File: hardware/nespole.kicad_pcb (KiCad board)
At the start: 2 copper layers, 26.4 x 50.5 mm, 20 parts, among them IC1 ATTINY25-20SSU, J1 Screw_Terminal_1x02, J2 Screw_Terminal_1x02, J3 ICSP, P1 USB_OTG, Q1 IRF510, U1 MAX31855KASA, U2 AP1117, U3 CH340G, Y1 12M

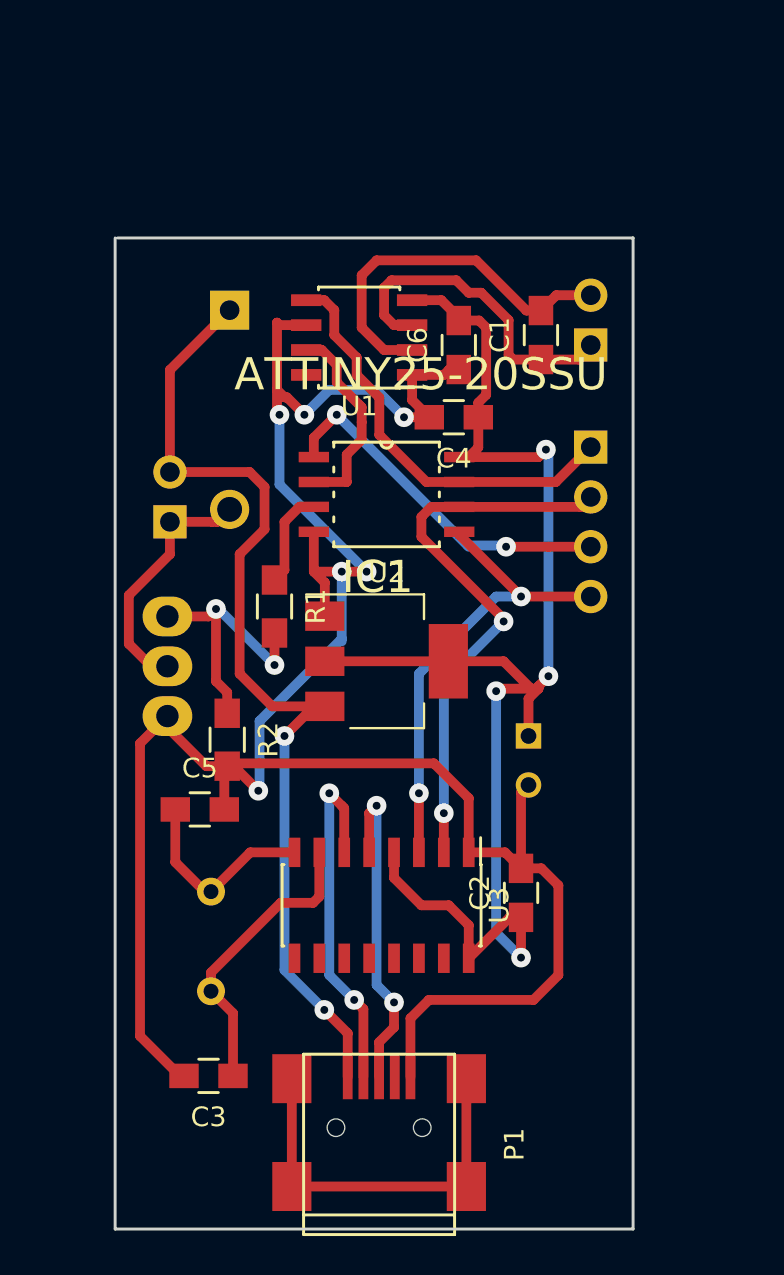
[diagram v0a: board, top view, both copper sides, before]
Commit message: Updating to use ATMEGA2313; I needed just one more pin :-(.
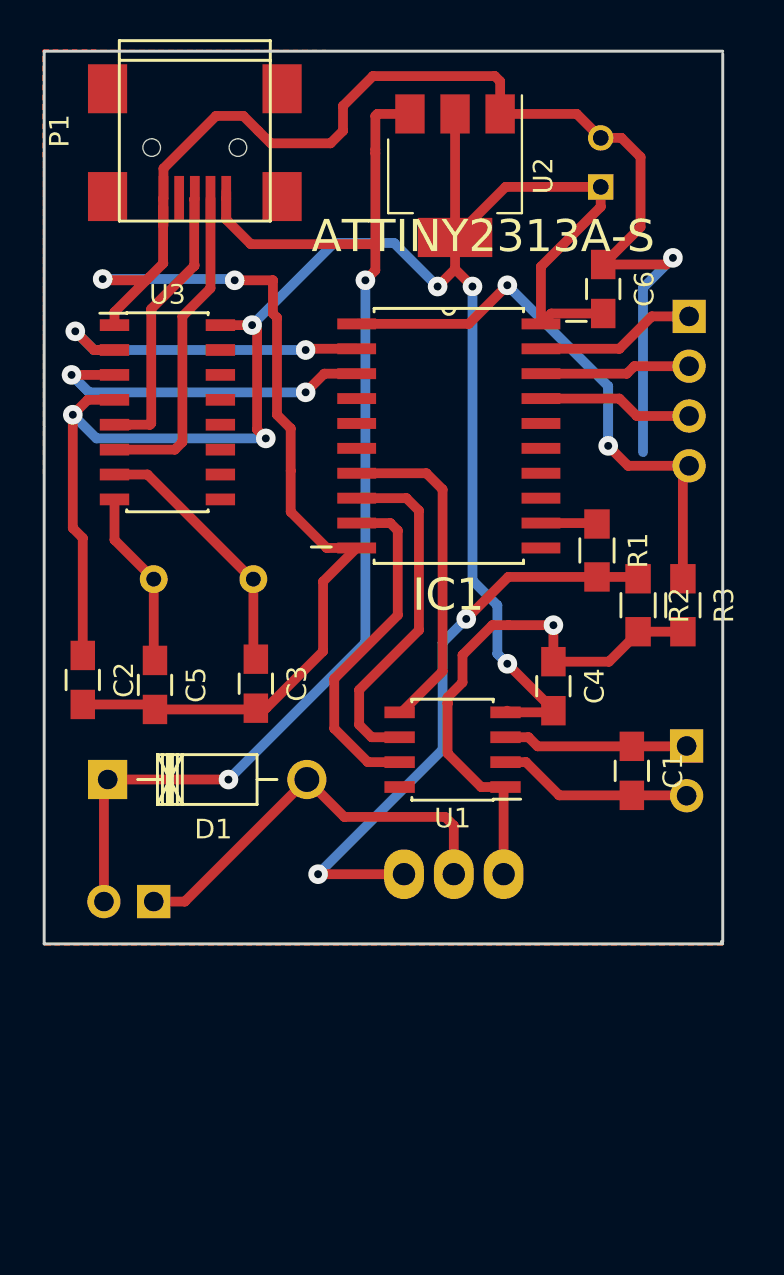
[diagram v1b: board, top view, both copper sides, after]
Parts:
- added R3: 10k, Resistors_SMD:R_0805_HandSoldering, F.Cu at (167.8, 98.6)
- D1: moved to F.Cu
- IC1: value ATTINY25-20SSU -> ATTINY2313A-S; footprint ATTINY25-20SU:SOIC127P798X216-8N -> ATTINY2313-20SU:SOIC127P1032X265-20N
- P1: footprint Connectors:USB_Mini-B -> nespole:USB_Mini-B
- Q1: value IRF510 -> MJE13009G
- moved P1 52.5 mm to (142.9, 74.4), turned to 270 degrees
- moved C7 28.2 mm to (163.6, 77.3), turned to 90 degrees
- moved U3 27.4 mm to (141.5, 88.8), turned to 0 degrees
- moved U2 25.0 mm to (156.1, 76.7), turned to 270 degrees
- moved C2 24.8 mm to (137.2, 102.4), turned to 270 degrees
- moved D1 24.7 mm to (138.4, 107.5), turned to 0 degrees
- moved C1 22.7 mm to (165.2, 107.1), turned to 270 degrees
- moved R2 22.0 mm to (165.5, 98.6)
- moved U1 21.6 mm to (156.0, 106.0)
- moved Y1 21.1 mm to (145.9, 97.3), turned to 180 degrees
- moved J1 21.0 mm to (168.0, 105.8), turned to 180 degrees
- moved C3 20.1 mm to (146.0, 102.6), turned to 270 degrees
- moved J2 19.4 mm to (140.8, 113.7), turned to 90 degrees
- moved Q1 18.0 mm to (156.1, 112.3), turned to 0 degrees
- moved R1 16.7 mm to (163.4, 95.8)
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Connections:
- C4 pad 1: +3V3 -> GND
- C4 pad 2: GND -> +3V3
- IC1 pad 1: Net-(IC1-Pad1) -> RESET
- IC1 pad 2: Net-(IC1-Pad2) -> /RX
- IC1 pad 3: Net-(IC1-Pad3) -> /TX
- IC1 pad 4: GND -> (no net)
- IC1 pad 5: Net-(IC1-Pad5) -> (no net)
- IC1 pad 6: Net-(IC1-Pad6) -> (no net)
- IC1 pad 7: Net-(IC1-Pad7) -> /THERMSCK
- IC1 pad 8: +3V3 -> /THERMCS
- J3 pad 1: Net-(IC1-Pad7) -> /SCK
- J3 pad 2: Net-(IC1-Pad6) -> /MISO
- J3 pad 3: Net-(IC1-Pad1) -> /MOSI
- J3 pad 4: Net-(IC1-Pad5) -> RESET
- P1 pad 4: Net-(P1-Pad4) -> (no net)
- P1 pad 6: Net-(P1-Pad6) -> (no net)
- R1 pad 1: Net-(IC1-Pad3) -> /ENABLE_RELAY
- U1 pad 5: Net-(IC1-Pad7) -> /THERMSCK
- U1 pad 6: GND -> /THERMCS
- U1 pad 7: Net-(IC1-Pad2) -> /THERMSO
- U3 pad 10: Net-(U3-Pad10) -> (no net)
- U3 pad 11: Net-(U3-Pad11) -> (no net)
- U3 pad 12: Net-(U3-Pad12) -> (no net)
- U3 pad 13: Net-(U3-Pad13) -> (no net)
- U3 pad 14: Net-(U3-Pad14) -> (no net)
- U3 pad 15: Net-(U3-Pad15) -> (no net)
- U3 pad 2: Net-(IC1-Pad6) -> /RX
- U3 pad 3: Net-(IC1-Pad5) -> /TX
- U3 pad 9: Net-(U3-Pad9) -> (no net)
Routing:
- net Net-(IC1-Pad6): track 29.3 -> 0.00 mm, vias 2 -> 0
- net RESET: track 0.00 -> 29.3 mm, vias 0 -> 2
- net +3V3: track 72.4 -> 101.6 mm, vias 4 -> 6
- net Net-(IC1-Pad5): track 24.5 -> 0.00 mm, vias 2 -> 0
- net Net-(IC1-Pad7): track 21.5 -> 0.00 mm
- net Net-(P1-Pad6): track 19.9 -> 0.00 mm
- net Net-(IC1-Pad1): track 18.5 -> 0.00 mm, vias 2 -> 0
- net /THERMCS: track 0.00 -> 17.9 mm
- net /THERMSO: track 0.00 -> 17.7 mm
- net /TX: track 0.00 -> 17.5 mm, vias 0 -> 2
- net /RX: track 0.00 -> 17.2 mm, vias 0 -> 2
- net /THERMSCK: track 0.00 -> 17.1 mm
- net Net-(Q1-Pad1): track 14.5 -> 30.5 mm
- net GND: track 121.6 -> 136.2 mm, vias 6 -> 4
- net Net-(IC1-Pad2): track 10.4 -> 0.00 mm
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- added copper zone on F.Cu, net GND
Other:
- board size 26.4 x 50.5 mm -> 34.6 x 45.5 mm

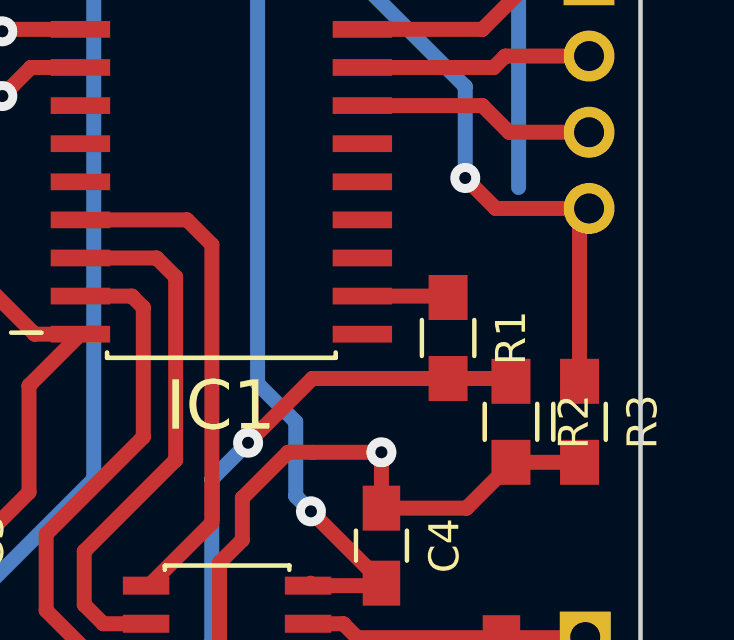
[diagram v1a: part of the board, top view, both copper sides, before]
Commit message: Just drive the relay directly...this MAX31855 is just not working properly.
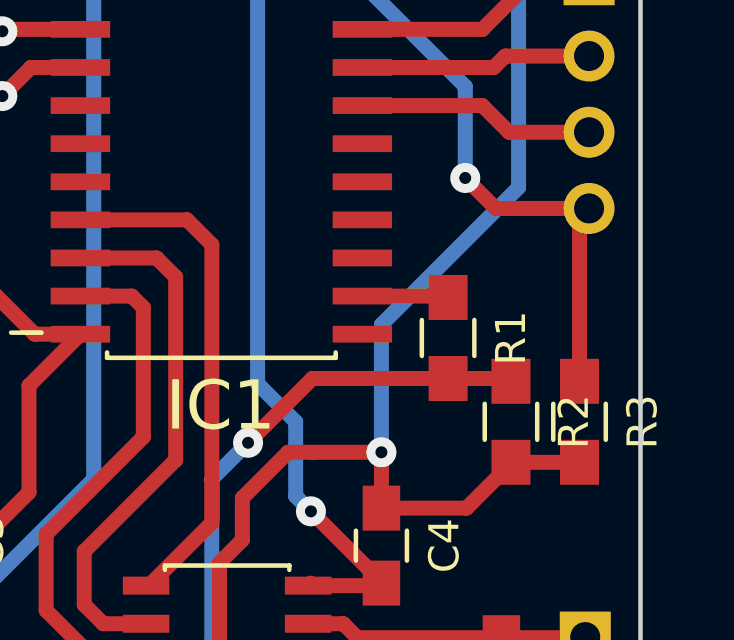
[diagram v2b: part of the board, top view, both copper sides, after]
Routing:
- net GND: track 136.2 -> 146.9 mm
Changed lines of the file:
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@@
   (general
     (links 50)
-    (no_connects 1)
+    (no_connects 0)
     (area 133.9025 69.146999 176.384881 122.155881)
     (thickness 1.6)
     (drawings 6)
-    (tracks 239)
+    (tracks 241)
     (zones 0)
     (modules 21)
@@
   (gr_line (start 135.1915 70.358) (end 169.799 70.358) (angle 90) (layer Edge.Cuts) (width 0.15))
   (gr_line (start 135.1915 89.4715) (end 135.1915 70.358) (angle 90) (layer Edge.Cuts) (width 0.15))
+  (segment (start 161.163 99.6315) (end 161.163 95.377) (width 0.5) (layer B.Cu) (net 1))
+  (segment (start 165.735 90.805) (end 165.735 82.423) (width 0.5) (layer B.Cu) (net 1))
+  (segment (start 165.735 82.423) (end 167.259 80.899) (width 0.5) (layer B.Cu) (net 1))
+  (via (at 167.259 80.899) (size 1) (drill 0.4) (layers F.Cu B.Cu) (net 1))
+  (segment (start 167.259 80.899) (end 166.9215 81.2365) (width 0.5) (layer F.Cu) (net 1))
+  (segment (start 166.9215 81.2365) (end 163.703 81.2365) (width 0.5) (layer F.Cu) (net 1) (status 10))
   (via (at 161.163 99.6315) (size 1) (drill 0.4) (layers F.Cu B.Cu) (net 1))
-  (segment (start 166.9215 81.2365) (end 163.703 81.2365) (width 0.5) (layer F.Cu) (net 1) (status 10))
-  (segment (start 167.259 80.899) (end 166.9215 81.2365) (width 0.5) (layer F.Cu) (net 1))
-  (via (at 167.259 80.899) (size 1) (drill 0.4) (layers F.Cu B.Cu) (net 1))
-  (segment (start 165.735 82.423) (end 167.259 80.899) (width 0.5) (layer B.Cu) (net 1))
-  (segment (start 165.735 90.805) (end 165.735 82.423) (width 0.5) (layer B.Cu) (net 1))
+  (segment (start 161.163 95.377) (end 165.735 90.805) (width 0.5) (layer B.Cu) (net 1))
   (segment (start 155.7655 103.632) (end 155.7655 103.3145) (width 0.5) (layer F.Cu) (net 1))
   (segment (start 158.877 99.6315) (end 161.163 99.6315) (width 0.5) (layer F.Cu) (net 1))
@@
   (segment (start 145.923 103.9295) (end 145.9865 103.866) (width 0.5) (layer F.Cu) (net 1) (status 30))
   (segment (start 163.576 74.7795) (end 164.632 74.7795) (width 0.5) (layer F.Cu) (net 1) (status 10))
+  (segment (start 165.608 79.3315) (end 163.703 81.2365) (width 0.5) (layer F.Cu) (net 1) (status 20))
+  (segment (start 165.608 75.7555) (end 165.608 79.3315) (width 0.5) (layer F.Cu) (net 1))
   (segment (start 164.632 74.7795) (end 165.608 75.7555) (width 0.5) (layer F.Cu) (net 1))
-  (segment (start 165.608 75.7555) (end 165.608 79.3315) (width 0.5) (layer F.Cu) (net 1))
-  (segment (start 165.608 79.3315) (end 163.703 81.2365) (width 0.5) (layer F.Cu) (net 1) (status 20))
   (segment (start 158.4465 73.558) (end 162.3545 73.558) (width 0.5) (layer F.Cu) (net 1) (status 10))
   (segment (start 162.3545 73.558) (end 163.576 74.7795) (width 0.5) (layer F.Cu) (net 1) (status 20))

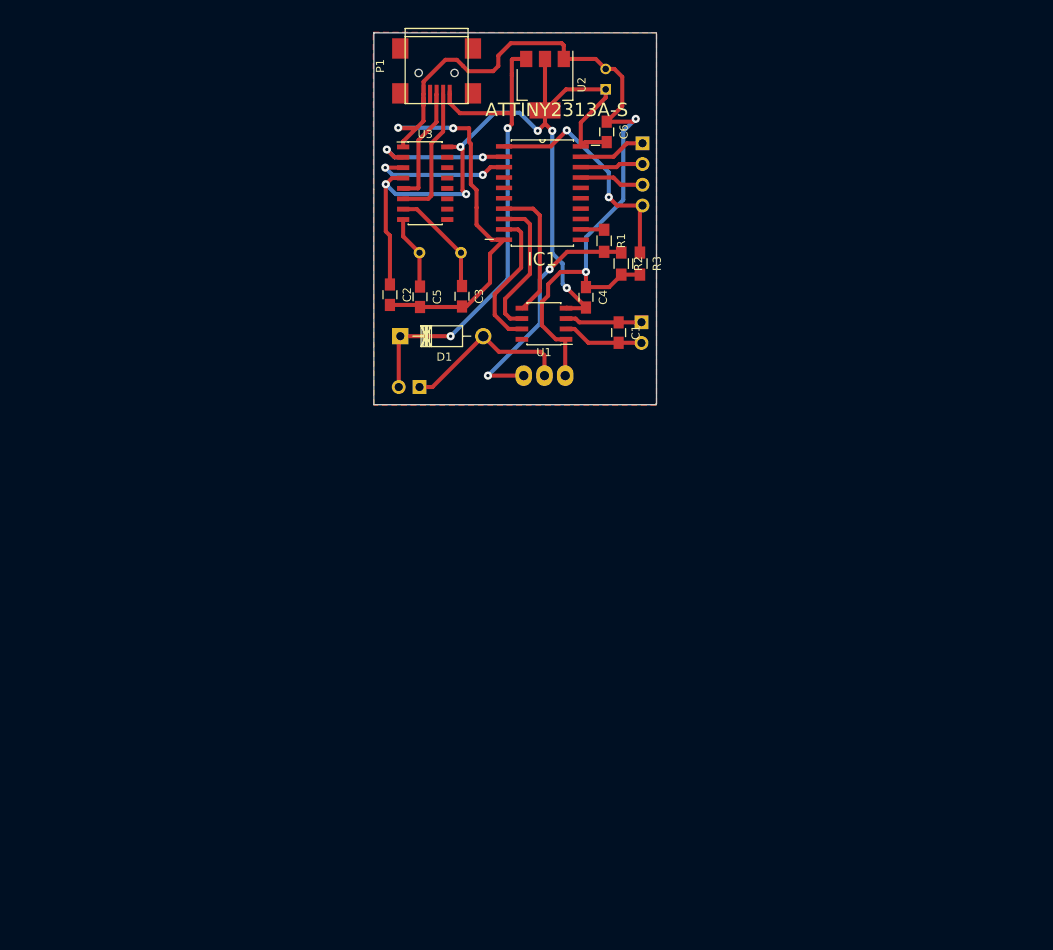
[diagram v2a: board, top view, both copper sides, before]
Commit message: Updating hardware for new display.
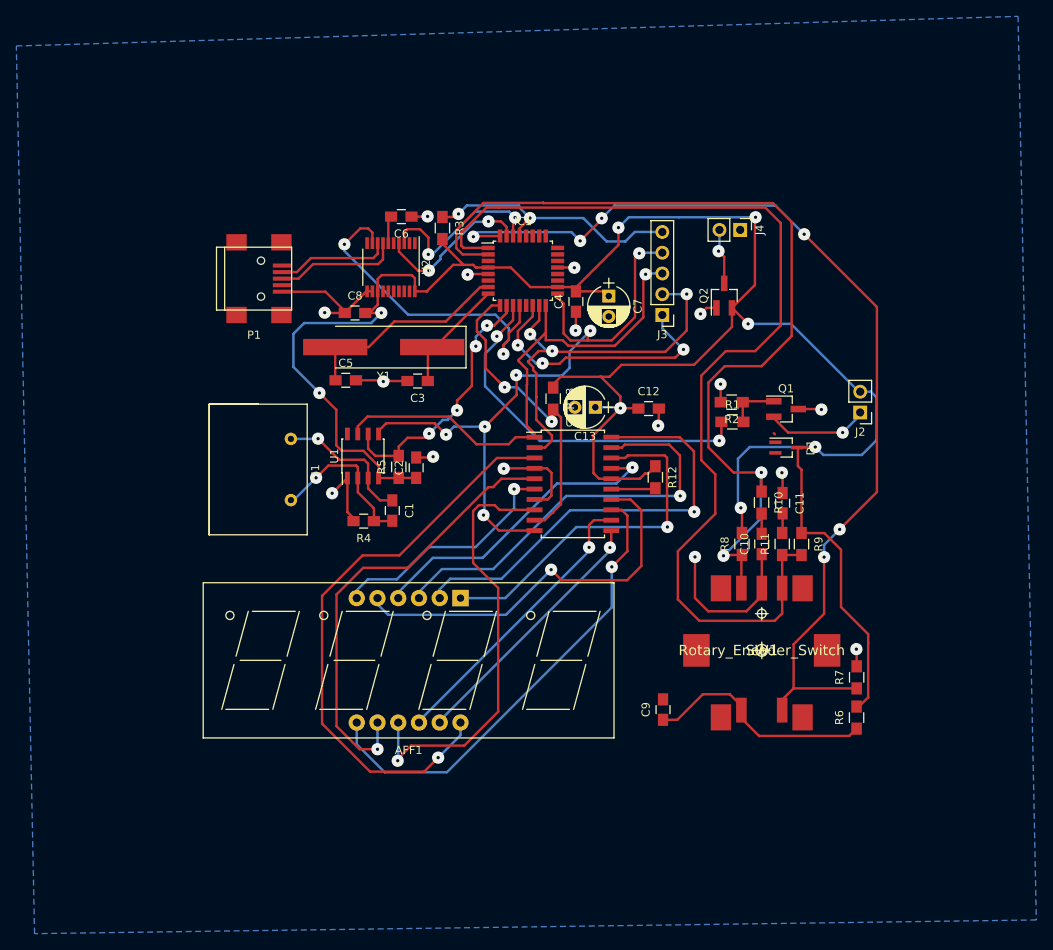
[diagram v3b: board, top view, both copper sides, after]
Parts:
- added AFF1: CA56-12, Displays_7-Segment:Cx56-12, F.Cu at (145.8, 139.6)
- added C10: 0.1u, Capacitors_SMD:C_0805_HandSoldering, F.Cu at (182.7, 132.9)
- added C11: 0.1u, Capacitors_SMD:C_0805_HandSoldering, F.Cu at (185.2, 128.0)
- added C12: 0.1uF, Capacitors_SMD:C_0805_HandSoldering, F.Cu at (168.8, 116.4)
- added C13: 10u, Capacitors_THT:CP_Radial_D5.0mm_P2.50mm, F.Cu at (162.3, 116.2)
- added C8: 0.1u, Capacitors_SMD:C_0805_HandSoldering, F.Cu at (132.9, 104.7)
- added C9: 0.1u, Capacitors_SMD:C_0805_HandSoldering, F.Cu at (170.6, 153.2)
- added J4: Screw_Terminal_1x02, Pin_Headers:Pin_Header_Straight_1x02_Pitch2.54mm, F.Cu at (180.0, 94.5)
- added Q2: MOSFET_P_CH, nespole:SOT-23_Handsoldering, F.Cu at (178.1, 102.5)
- added R10: 2.2k, Resistors_SMD:R_0805_HandSoldering, F.Cu at (182.7, 127.9)
- added R11: 2.2k, Resistors_SMD:R_0805_HandSoldering, F.Cu at (185.2, 132.9)
- added R12: 9.53k, Resistors_SMD:R_0805_HandSoldering, F.Cu at (169.7, 124.8)
- added R13: 10k, Resistors_SMD:R_0805_HandSoldering, F.Cu at (157.1, 115.2)
- added R4: 0, Capacitors_SMD:C_0805_HandSoldering, F.Cu at (133.9, 130.1)
- added R5: 10k, Resistors_SMD:R_0805_HandSoldering, F.Cu at (138.2, 123.5)
- added R6: 1k, Resistors_SMD:R_0805_HandSoldering, F.Cu at (194.3, 154.2)
- added R7: 10k, Resistors_SMD:R_0805_HandSoldering, F.Cu at (194.3, 149.3)
- added R8: 10k, Resistors_SMD:R_0805_HandSoldering, F.Cu at (180.3, 132.9)
- added R9: 10k, Resistors_SMD:R_0805_HandSoldering, F.Cu at (187.6, 133.0)
- added SW1: Rotary_Encoder_Switch, nespole:ROTARY-ENCODER-PEC11S, F.Cu at (182.7, 146.0)
- C7: footprint Capacitors_THT:C_Radial_D5_L6_P2.5 -> Capacitors_THT:CP_Radial_D5.0mm_P2.50mm; moved to F.Cu
- D1: footprint Diodes_THT:Diode_DO-41_SOD81_Horizontal_RM10 -> nespole:SOT-323_DIODE
- IC1: value ATTINY2313A-S -> ATMEGA328PB-A; footprint ATTINY2313-20SU:SOIC127P1032X265-20N -> Housings_QFP:TQFP-32_7x7mm_Pitch0.8mm
- J1: footprint Pin_Headers:Pin_Header_Straight_1x02_Pitch2.54mm -> nespole:01x02_7.5mm_Header_Screw_Terminal; moved to F.Cu
- J2: moved to F.Cu
- J3: value ICSP -> Screw_Terminal_1x05; footprint Pin_Headers:Pin_Header_Straight_1x04_Pitch2.54mm -> Pin_Headers:Pin_Header_Straight_1x05_Pitch2.54mm; moved to F.Cu
- Q1: footprint Power_Integrations:TO-220 -> TO_SOT_Packages_SMD:SOT-23_Handsoldering; moved to F.Cu
- U1: value MAX31855KASA -> MAX6675
- U2: value AP1117 -> CH341T; footprint TO_SOT_Packages_SMD:SOT-223 -> Housings_SSOP:TSSOP-20_4.4x6.5mm_Pitch0.65mm
- U3: value CH340G -> AS1108; footprint Housings_SOIC:SOIC-16_3.9x9.9mm_Pitch1.27mm -> Housings_SOIC:SOIC-20W_7.5x12.8mm_Pitch1.27mm
- Y1: footprint Crystals:HC-49V -> Crystals:Crystal_SMD_HC49-SD_HandSoldering; moved to F.Cu
- moved J2 54.1 mm to (194.7, 116.8), turned to 180 degrees
- moved J1 50.3 mm to (121.0, 123.8), turned to 270 degrees
- moved D1 49.2 mm to (185.7, 121.1), turned to 270 degrees
- moved U3 41.0 mm to (159.6, 125.6)
- moved C1 35.3 mm to (137.5, 128.9)
- moved P1 34.3 mm to (120.5, 100.5), turned to 0 degrees
- moved Q1 29.9 mm to (185.7, 116.4)
- moved U2 29.2 mm to (137.3, 99.1)
- moved U1 27.4 mm to (133.9, 122.2), turned to 90 degrees
- moved C6 27.2 mm to (138.6, 92.9), turned to 180 degrees
- moved R1 27.2 mm to (179.1, 118.0), turned to 0 degrees
- moved C7 25.3 mm to (164.0, 102.6), turned to 270 degrees
- moved R3 24.6 mm to (143.6, 94.3)
- moved R2 21.7 mm to (179.0, 115.6), turned to 180 degrees
- moved C2 21.4 mm to (140.4, 123.6), turned to 90 degrees
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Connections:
- C2 pad 1: +3V3 -> +5V
- C4 pad 2: +3V3 -> +5V
- C6 pad 2: +3V3 -> Net-(C6-Pad2)
- C7 pad 1: +3V3 -> +5V
- IC1 pad 1: RESET -> SW_INT
- IC1 pad 10: GND -> TEMP_CS
- IC1 pad 11: (no net) -> ENABLE_RELAY
- IC1 pad 12: /ENABLE_RELAY -> CLKOUT
- IC1 pad 13: (no net) -> Net-(IC1-Pad13)
- IC1 pad 14: (no net) -> MC_CS
- IC1 pad 15: (no net) -> MOSI
- IC1 pad 16: (no net) -> MISO
- IC1 pad 17: /MOSI -> SCK
- IC1 pad 18: /MISO -> +5V
- IC1 pad 19: /SCK -> Net-(IC1-Pad19)
- IC1 pad 2: /RX -> SW_DIR
- IC1 pad 20: +3V3 -> Net-(IC1-Pad20)
- IC1 pad 3: /TX -> Net-(IC1-Pad3)
- IC1 pad 4: (no net) -> +5V
- IC1 pad 5: (no net) -> GND
- IC1 pad 6: (no net) -> Net-(IC1-Pad6)
- IC1 pad 7: /THERMSCK -> Net-(C5-Pad1)
- IC1 pad 8: /THERMCS -> Net-(C3-Pad1)
- IC1 pad 9: /THERMSO -> LED_CS
- J3 pad 1: /SCK -> MC_CS
- J3 pad 2: /MISO -> MOSI
- J3 pad 3: /MOSI -> MISO
- J3 pad 4: RESET -> SCK
- P1 pad 1: +5V -> Net-(P1-Pad1)
- P1 pad 4: (no net) -> Net-(P1-Pad4)
- P1 pad 6: (no net) -> Net-(P1-Pad6)
- R1 pad 1: /ENABLE_RELAY -> ENABLE_RELAY
- R3 pad 2: GND -> +5V
- U1 pad 4: +3V3 -> +5V
- U1 pad 5: /THERMSCK -> SCK
- U1 pad 6: /THERMCS -> TEMP_CS
- U1 pad 7: /THERMSO -> MISO
- U2 pad 1: GND -> Net-(U2-Pad1)
- U2 pad 2: +3V3 -> Net-(U2-Pad2)
- U2 pad 3: +5V -> RXD
- U2 pad 4: +3V3 -> TXD
- U3 pad 1: GND -> MISO
- U3 pad 10: (no net) -> SCK
- U3 pad 11: (no net) -> Net-(AFF1-Pad11)
- U3 pad 12: (no net) -> Net-(AFF1-Pad10)
- U3 pad 13: (no net) -> Net-(AFF1-Pad7)
- U3 pad 14: (no net) -> Net-(AFF1-Pad5)
- U3 pad 15: (no net) -> Net-(R12-Pad2)
- U3 pad 16: +3V3 -> +5V
- U3 pad 2: /RX -> MOSI
- U3 pad 3: /TX -> Net-(AFF1-Pad12)
- U3 pad 4: +3V3 -> GND
- U3 pad 5: Net-(P1-Pad3) -> Net-(AFF1-Pad8)
- U3 pad 6: Net-(P1-Pad2) -> Net-(AFF1-Pad6)
- U3 pad 7: Net-(C3-Pad1) -> GND
- U3 pad 8: Net-(C5-Pad1) -> Net-(AFF1-Pad9)
- U3 pad 9: (no net) -> LED_CS
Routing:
- net +5V: track 61.3 -> 276.7 mm, vias 2 -> 8
- net SW_INT: track 0.00 -> 124.7 mm
- net SW_BUTTON: track 0.00 -> 122.3 mm, vias 0 -> 6
- net SW_DIR: track 0.00 -> 113.0 mm, vias 0 -> 2
- net +3V3: track 101.6 -> 0.00 mm, vias 6 -> 0
- net SCK: track 0.00 -> 81.0 mm, vias 0 -> 6
- net Net-(AFF1-Pad12): track 0.00 -> 71.4 mm, vias 0 -> 1
- net MISO: track 0.00 -> 65.2 mm, vias 0 -> 1
- net GND: track 146.9 -> 86.5 mm, vias 4 -> 16
- net Net-(AFF1-Pad7): track 0.00 -> 58.0 mm, vias 0 -> 1
- net Net-(AFF1-Pad8): track 0.00 -> 55.7 mm, vias 0 -> 1
- net Net-(AFF1-Pad2): track 0.00 -> 54.6 mm, vias 0 -> 1
- net Net-(AFF1-Pad9): track 0.00 -> 53.5 mm, vias 0 -> 1
- net Net-(AFF1-Pad3): track 0.00 -> 51.7 mm, vias 0 -> 1
- net MOSI: track 0.00 -> 49.5 mm, vias 0 -> 3
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- added copper zone on B.Cu, net GND
- removed copper zone on F.Cu, net GND
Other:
- board outline removed
- net class Default: clearance 0.4 -> 0.25; trace_width 0.5 -> 0.3; via_dia 1 -> 1.5
- rule trace_clearance: 0.4 -> 0.25
